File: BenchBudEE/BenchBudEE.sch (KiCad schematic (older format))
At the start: 0 parts

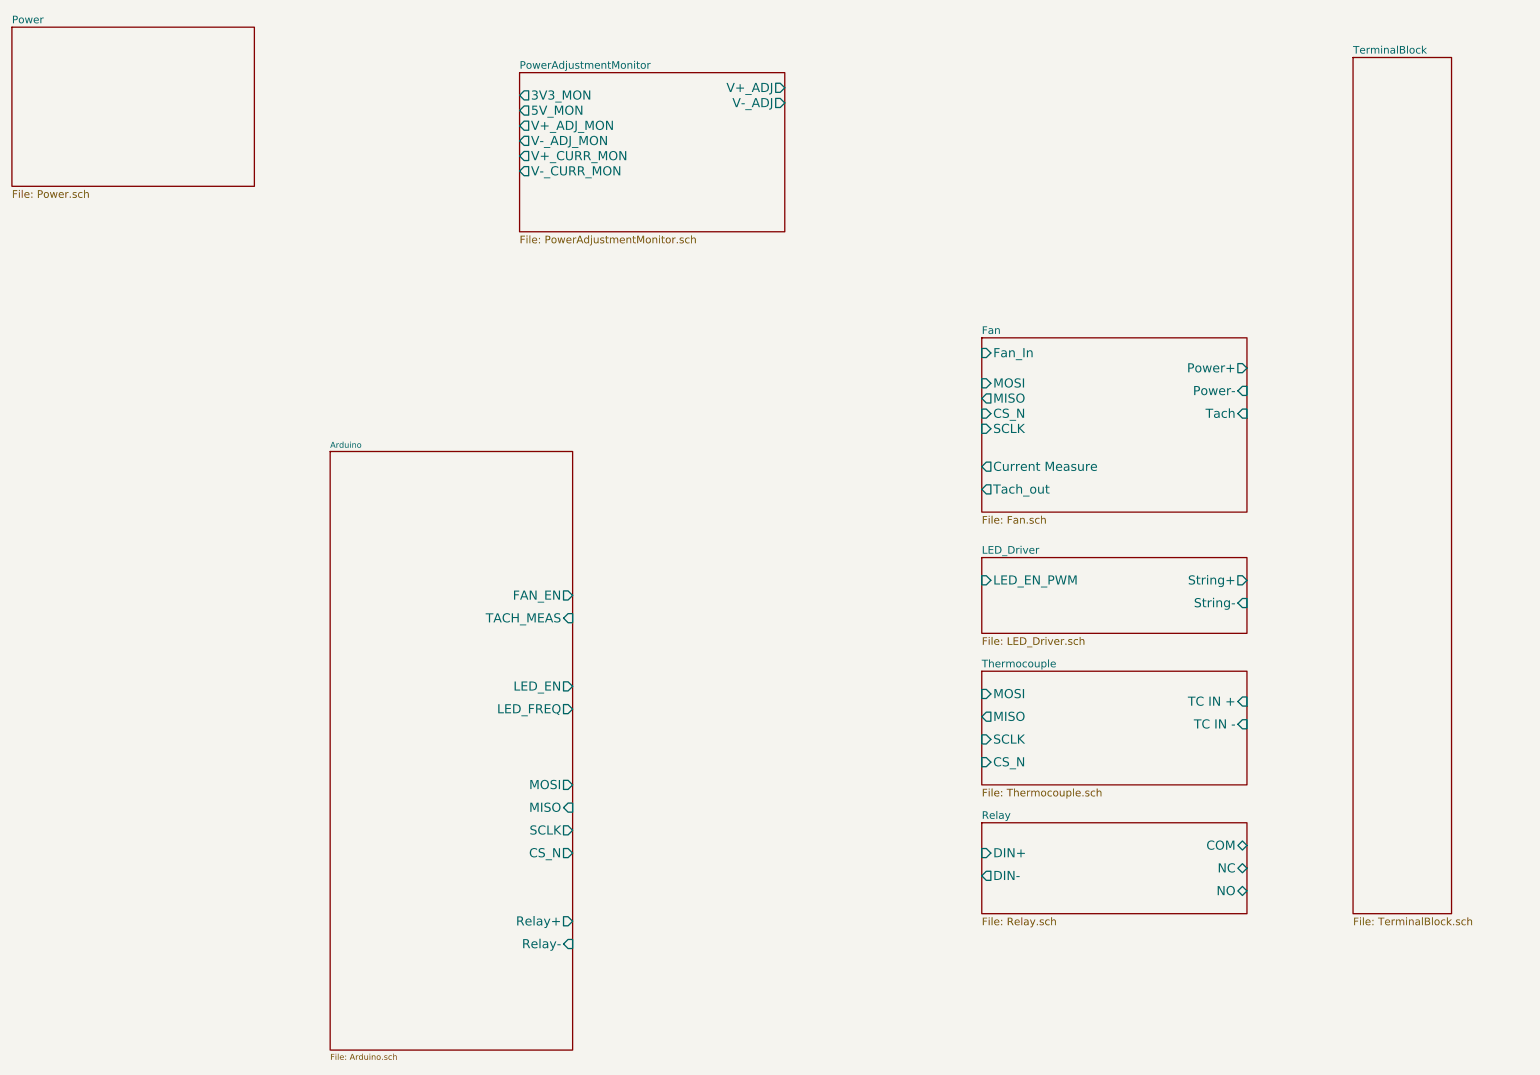
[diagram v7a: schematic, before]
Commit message: Arduino block diagram
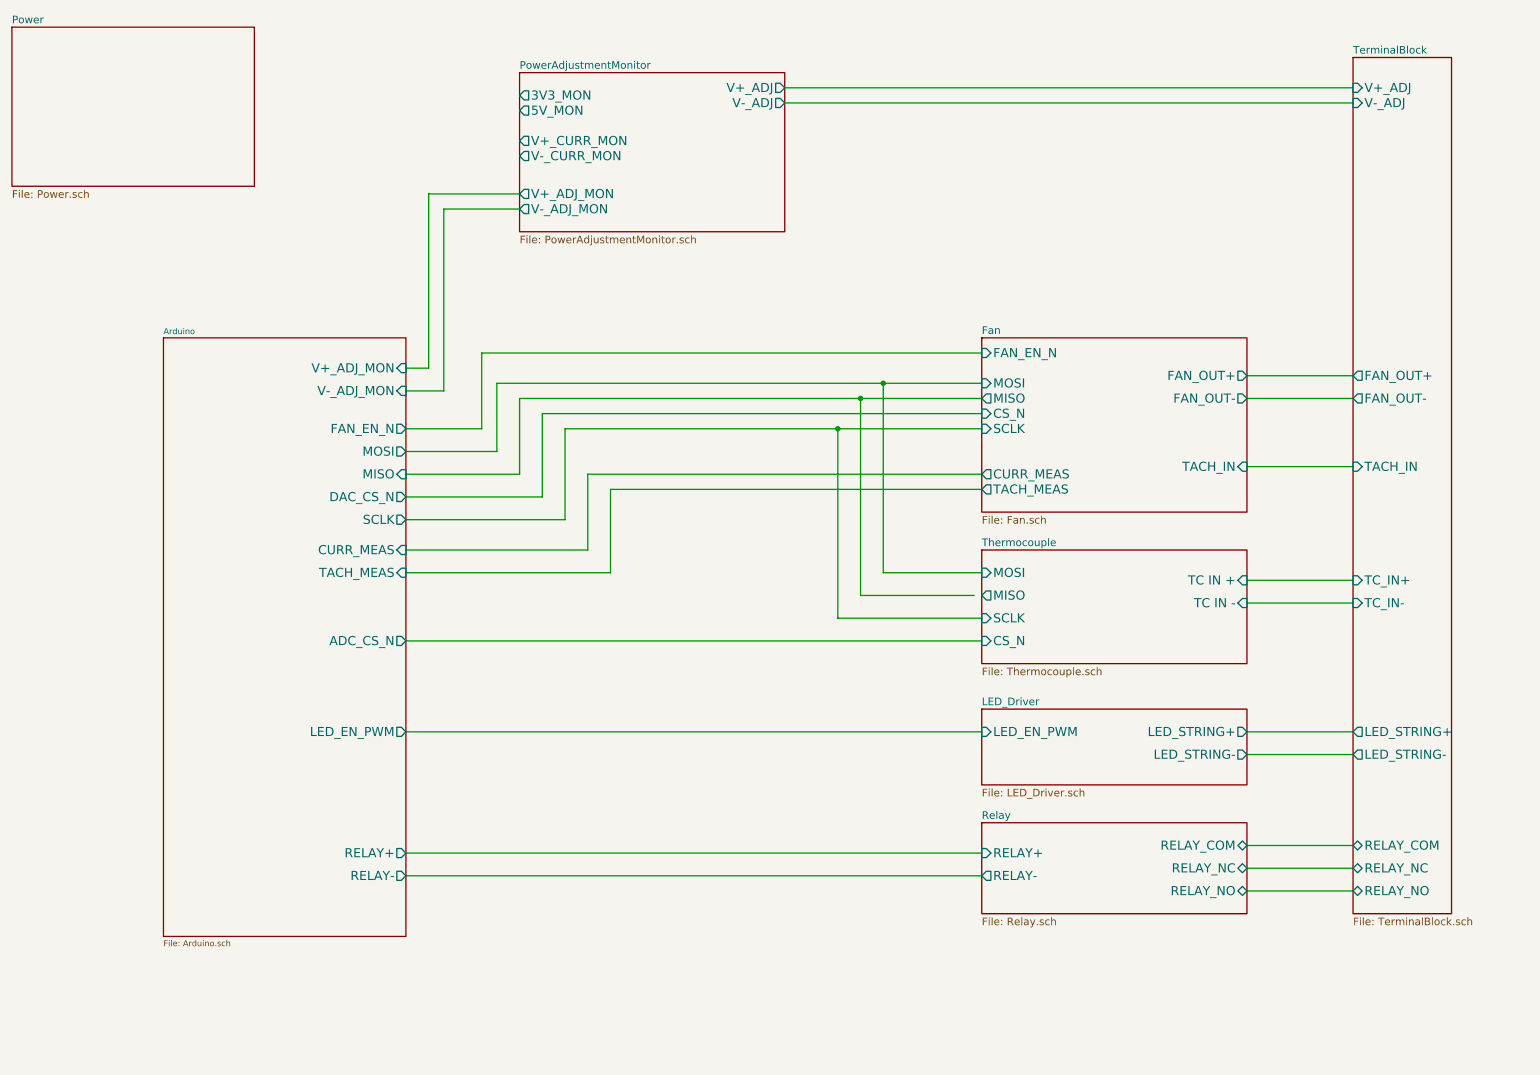
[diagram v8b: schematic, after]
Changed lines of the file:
@@
 $EndDescr
 $Sheet
-S 2800 3500 1600 3950
-U 52ED1BFA
-F0 "Arduino" 39
-F1 "Arduino.sch" 39
-F2 "Relay+" O R 4400 6600 60
-F3 "Relay-" I R 4400 6750 60
-F4 "MOSI" O R 4400 5700 60
-F5 "MISO" I R 4400 5850 60
-F6 "SCLK" O R 4400 6000 60
-F7 "CS_N" O R 4400 6150 60
-F8 "LED_EN" O R 4400 5050 60
-F9 "LED_FREQ" O R 4400 5200 60
-F10 "FAN_EN" O R 4400 4450 60
-F11 "TACH_MEAS" I R 4400 4600 60
-$EndSheet
-$Sheet
-S 7100 4950 1750 750
+S 7100 4150 1750 750
 U 52ED1C3D
 F0 "Thermocouple" 50
 F1 "Thermocouple.sch" 50
-F2 "TC IN +" I R 8850 5150 60
-F3 "TC IN -" I R 8850 5300 60
-F4 "MOSI" I L 7100 5100 60
-F5 "MISO" O L 7100 5250 60
-F6 "SCLK" I L 7100 5400 60
-F7 "CS_N" I L 7100 5550 60
-$EndSheet
-$Sheet
-S 7100 4200 1750 500
+F2 "TC IN +" I R 8850 4350 60
+F3 "TC IN -" I R 8850 4500 60
+F4 "MOSI" I L 7100 4300 60
+F5 "MISO" O L 7100 4450 60
+F6 "SCLK" I L 7100 4600 60
+F7 "CS_N" I L 7100 4750 60
+$EndSheet
+$Sheet
+S 7100 5200 1750 500
 U 52ED1C90
 F0 "LED_Driver" 50
 F1 "LED_Driver.sch" 50
-F2 "String+" O R 8850 4350 60
-F3 "String-" I R 8850 4500 60
-F4 "LED_EN_PWM" I L 7100 4350 60
+F2 "LED_EN_PWM" I L 7100 5350 60
+F3 "LED_STRING+" O R 8850 5350 60
+F4 "LED_STRING-" O R 8850 5500 60
+$EndSheet
+$Sheet
+S 700  700  1600 1050
+U 52ED1C5C
+F0 "Power" 50
+F1 "Power.sch" 50
+$EndSheet
+$Sheet
+S 7100 5950 1750 600
+U 52ED1C4D
+F0 "Relay" 50
+F1 "Relay.sch" 50
+F2 "RELAY_NC" B R 8850 6250 60
+F3 "RELAY_NO" B R 8850 6400 60
+F4 "RELAY_COM" B R 8850 6100 60
+F5 "RELAY+" I L 7100 6150 60
+F6 "RELAY-" O L 7100 6300 60
 $EndSheet
 $Sheet
@@
 F0 "Fan" 50
 F1 "Fan.sch" 50
-F2 "Power+" O R 8850 2950 60
-F3 "Power-" I R 8850 3100 60
-F4 "Tach" I R 8850 3250 60
-F5 "Tach_out" O L 7100 3750 60
-F6 "Fan_In" I L 7100 2850 60
-F7 "Current Measure" O L 7100 3600 60
-F8 "MOSI" I L 7100 3050 60
-F9 "MISO" O L 7100 3150 60
-F10 "CS_N" I L 7100 3250 60
-F11 "SCLK" I L 7100 3350 60
+F2 "MOSI" I L 7100 3050 60
+F3 "MISO" O L 7100 3150 60
+F4 "CS_N" I L 7100 3250 60
+F5 "SCLK" I L 7100 3350 60
+F6 "FAN_OUT+" O R 8850 3000 60
+F7 "TACH_IN" I R 8850 3600 60
+F8 "TACH_MEAS" O L 7100 3750 60
+F9 "FAN_EN_N" I L 7100 2850 60
+F10 "CURR_MEAS" O L 7100 3650 60
+F11 "FAN_OUT-" O R 8850 3150 60
 $EndSheet
 $Sheet
@@
 F0 "TerminalBlock" 50
 F1 "TerminalBlock.sch" 50
-$EndSheet
+F2 "V+_ADJ" I L 9550 1100 60
+F3 "V-_ADJ" I L 9550 1200 60
+F4 "TACH_IN" I L 9550 3600 60
+F5 "LED_STRING+" O L 9550 5350 60
+F6 "LED_STRING-" O L 9550 5500 60
+F7 "TC_IN+" I L 9550 4350 60
+F8 "TC_IN-" I L 9550 4500 60
+F9 "RELAY_COM" B L 9550 6100 60
+F10 "RELAY_NC" B L 9550 6250 60
+F11 "RELAY_NO" B L 9550 6400 60
+F12 "FAN_OUT+" O L 9550 3000 60
+F13 "FAN_OUT-" O L 9550 3150 60
+$EndSheet
+Wire Wire Line
+	5800 1100 9550 1100
+Wire Wire Line
+	9550 1200 5800 1200
+Wire Wire Line
+	8850 3000 9550 3000
+Wire Wire Line
+	9550 3150 8850 3150
+Wire Wire Line
+	8850 3600 9550 3600
+Wire Wire Line
+	8850 6100 9550 6100
+Wire Wire Line
+	9550 6250 8850 6250
+Wire Wire Line
+	8850 6400 9550 6400
+$Sheet
+S 1700 2750 1600 3950
+U 52ED1BFA
+F0 "Arduino" 39
+F1 "Arduino.sch" 39
+F2 "MOSI" O R 3300 3500 60
+F3 "MISO" I R 3300 3650 60
+F4 "SCLK" O R 3300 3950 60
+F5 "TACH_MEAS" I R 3300 4300 60
+F6 "RELAY+" O R 3300 6150 60
+F7 "RELAY-" O R 3300 6300 60
+F8 "FAN_EN_N" O R 3300 3350 60
+F9 "CURR_MEAS" I R 3300 4150 60
+F10 "V+_ADJ_MON" I R 3300 2950 60
+F11 "V-_ADJ_MON" I R 3300 3100 60
+F12 "LED_EN_PWM" O R 3300 5350 60
+F13 "DAC_CS_N" O R 3300 3800 60
+F14 "ADC_CS_N" O R 3300 4750 60
+$EndSheet
+Wire Wire Line
+	8850 4350 9550 4350
+Wire Wire Line
+	9550 4500 8850 4500
+Wire Wire Line
+	9550 5350 8850 5350
+Wire Wire Line
+	8850 5500 9550 5500
 $Sheet
 S 4050 1000 1750 1050
@@
 F4 "3V3_MON" O L 4050 1150 60
 F5 "5V_MON" O L 4050 1250 60
-F6 "V+_ADJ_MON" O L 4050 1350 60
-F7 "V-_ADJ_MON" O L 4050 1450 60
-F8 "V+_CURR_MON" O L 4050 1550 60
-F9 "V-_CURR_MON" O L 4050 1650 60
-$EndSheet
-$Sheet
-S 700  700  1600 1050
-U 52ED1C5C
-F0 "Power" 50
-F1 "Power.sch" 50
-$EndSheet
-$Sheet
-S 7100 5950 1750 600
-U 52ED1C4D
-F0 "Relay" 50
-F1 "Relay.sch" 50
-F2 "DIN+" I L 7100 6150 60
-F3 "DIN-" O L 7100 6300 60
-F4 "NC" B R 8850 6250 60
-F5 "NO" B R 8850 6400 60
-F6 "COM" B R 8850 6100 60
-$EndSheet
+F6 "V+_ADJ_MON" O L 4050 1800 60
+F7 "V-_ADJ_MON" O L 4050 1900 60
+F8 "V+_CURR_MON" O L 4050 1450 60
+F9 "V-_CURR_MON" O L 4050 1550 60
+$EndSheet
+Wire Wire Line
+	3300 2950 3450 2950
+Wire Wire Line
+	3450 2950 3450 1800
+Wire Wire Line
+	3450 1800 4050 1800
+Wire Wire Line
+	3550 1900 4050 1900
+Wire Wire Line
+	3550 1900 3550 3100
+Wire Wire Line
+	3550 3100 3300 3100
+Wire Wire Line
+	3300 3350 3800 3350
+Wire Wire Line
+	3800 3350 3800 2850
+Wire Wire Line
+	3800 2850 7100 2850
+Wire Wire Line
+	3300 3500 3900 3500
+Wire Wire Line
+	3900 3500 3900 3050
+Wire Wire Line
+	3900 3050 7100 3050
+Wire Wire Line
+	4050 3150 7100 3150
+Wire Wire Line
+	4050 3150 4050 3650
+Wire Wire Line
+	4050 3650 3300 3650
+Wire Wire Line
+	3300 3800 4200 3800
+Wire Wire Line
+	4200 3800 4200 3250
+Wire Wire Line
+	4200 3250 7100 3250
+Wire Wire Line
+	3300 3950 4350 3950
+Wire Wire Line
+	4350 3950 4350 3350
+Wire Wire Line
+	4350 3350 7100 3350
+Wire Wire Line
+	3300 4150 4500 4150
+Wire Wire Line
+	4500 4150 4500 3650
+Wire Wire Line
+	4500 3650 7100 3650
+Wire Wire Line
+	7100 3750 4650 3750
+Wire Wire Line
+	4650 3750 4650 4300
+Wire Wire Line
+	4650 4300 3300 4300
+Wire Wire Line
+	7100 4300 6450 4300
+Wire Wire Line
+	6450 4300 6450 3050
+Connection ~ 6450 3050
+Wire Wire Line
+	7050 4450 6300 4450
+Wire Wire Line
+	6300 4450 6300 3150
+Connection ~ 6300 3150
+Wire Wire Line
+	7100 4600 6150 4600
+Wire Wire Line
+	6150 4600 6150 3350
+Connection ~ 6150 3350
+Wire Wire Line
+	3300 4750 7100 4750
+Wire Wire Line
+	7100 6300 3300 6300
+Wire Wire Line
+	3300 6150 7100 6150
+Wire Wire Line
+	3300 5350 7100 5350
 $EndSCHEMATC
